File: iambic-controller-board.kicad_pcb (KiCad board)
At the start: 2 copper layers, 48.1 x 15 mm, 16 parts, among them J1 Header 1, J2 AudioJack3, J3 ISP Header, U1 USB_A_PCB, U2 ATtiny85-20S

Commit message: final rev1
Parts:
- added C2: 10uF, Capacitor_SMD:C_0603_1608Metric, F.Cu at (141.2, 103.2)
- D2, D3: value ~ -> BZT52C3V6S
- U1: footprint Custom_Lib:PCB_USB_connector -> Edge_USB_PCB:PCB_USB_A
- moved D1 7.95 mm to (140.6, 101.2)
- moved R1 7.95 mm to (141.5, 101.2)
- moved C1 7.90 mm to (142.3, 104.8)
- moved D3 7.69 mm to (138.3, 99.9), turned to -90 degrees
- moved D4 7.64 mm to (150.3, 106.2)
- moved D5 7.64 mm to (152.3, 106.2)
- moved J1 7.64 mm to (150.2, 96.4)
- moved J2 7.64 mm to (166.7, 102.1)
- moved J3 7.64 mm to (141.2, 107.6)
- moved R2 7.64 mm to (140.9, 99.6)
- moved R3 7.64 mm to (140.9, 98.7)
- moved R4 7.64 mm to (150.3, 108.0)
- moved R5 7.64 mm to (152.3, 108.0)
- moved U2 7.64 mm to (148.5, 102.1)
- moved D2 6.90 mm to (139.3, 98.5)
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- renumbered C5 to C1
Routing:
- net GND: track 73.1 -> 0.12 mm, vias 5 -> 28
- net Net-(D3-K): track 15.9 -> 11.7 mm
- net Net-(D2-K): track 13.4 -> 9.44 mm
- net Net-(D1-A): track 14.2 -> 10.5 mm
- net /MISO: track 24.7 -> 22.4 mm, vias 2 -> 4
- net /AUDIO_TIP: track 34.4 -> 35.7 mm, vias 4 -> 6
- net /USB_DN: track 16.0 -> 16.9 mm, vias 2 -> 1
- net /AUDIO_RING: track 23.8 -> 24.6 mm
- net /USB_DP: track 14.3 -> 14.6 mm, vias 2 -> 0
- net /RESET: track 33.9 -> 33.8 mm, vias 3 -> 6
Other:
- board size 48.1 x 15 mm -> 44.9 x 15 mm
- board text added: "1"
- board text added: "2"
- board text added: "3"
- board text added: "4"
- board text added: "5"
- board text added: "6"
- board text added: "GND"
- board text added: "Iambic Paddle Controller"
- board text added: "P1 RESET"
- board text added: "P2 USB+ ADC2"
- board text added: "P3 USB- ADC3"
- board text added: "P4 MISO DO PWM AIN1"
- board text added: "R"
- board text added: "S"
- board text added: "T"
- board text added: "WayWayWay"
- board text added: "dbstreif"
- board text added: "rev1"

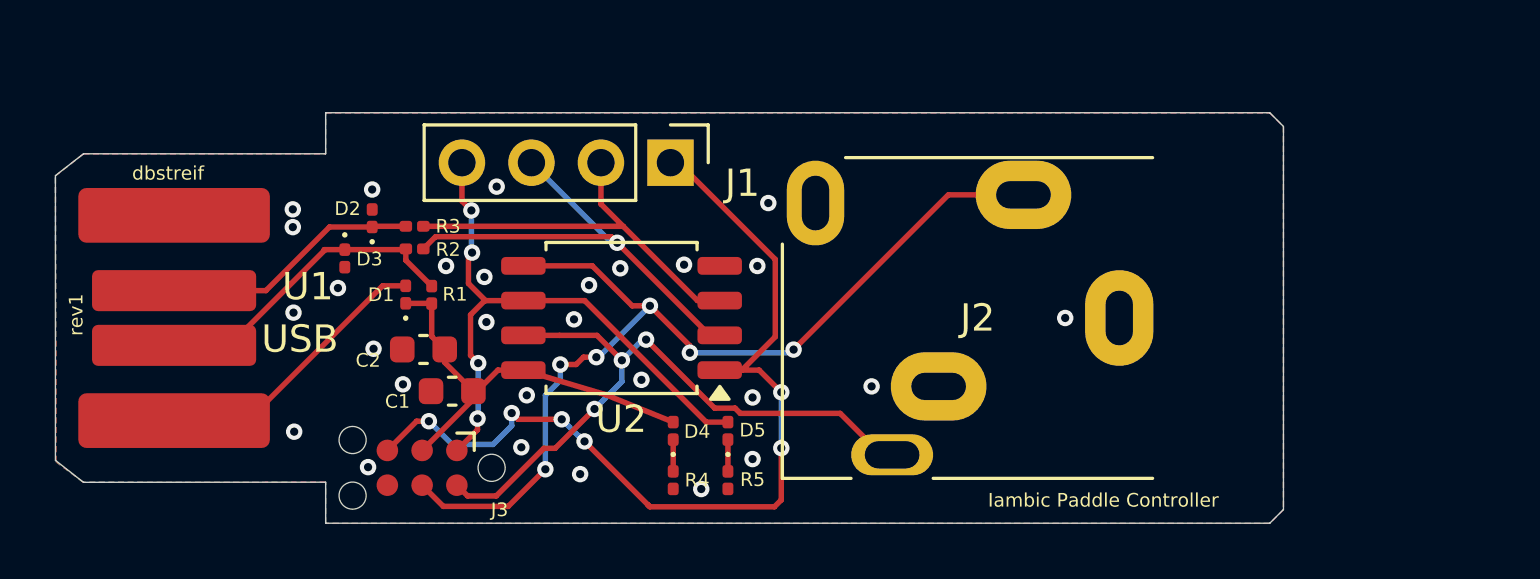
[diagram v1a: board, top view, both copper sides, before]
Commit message: Fixed weird footprints
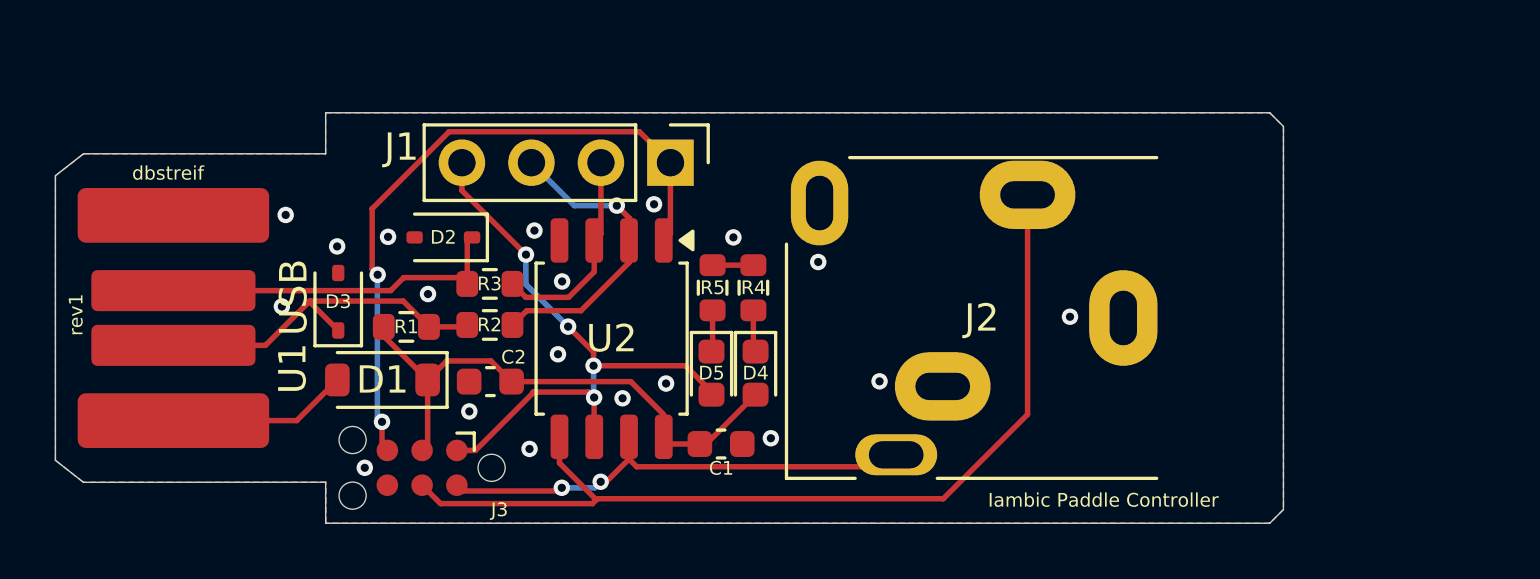
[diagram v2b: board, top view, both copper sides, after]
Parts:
- D1: footprint Diode_SMD:D_0201_0603Metric -> Diode_SMD:D_SOD-123
- D2, D3: value BZT52C3V6S -> 3V6; footprint Diode_SMD:D_0201_0603Metric -> Diode_SMD:D_SOD-323
- D4, D5: footprint LED_SMD:LED_0201_0603Metric -> LED_SMD:LED_0603_1608Metric
- R1, R2, R3, R4, R5: footprint Resistor_SMD:R_0201_0603Metric -> Resistor_SMD:R_0603_1608Metric
- moved C1 10.0 mm to (152.1, 106.7), turned to 180 degrees
- moved R4 7.62 mm to (153.3, 101.0), turned to 90 degrees
- moved R5 7.05 mm to (151.8, 101.0), turned to 90 degrees
- moved R2 3.91 mm to (143.7, 102.3)
- moved D4 3.68 mm to (153.4, 104.1), turned to -90 degrees
- moved R3 3.46 mm to (143.7, 100.8)
- moved D1 3.23 mm to (139.7, 104.4), turned to 180 degrees
- moved C2 2.71 mm to (143.7, 104.4)
- moved D2 2.69 mm to (141.9, 99.2), turned to 180 degrees
- moved D5 2.19 mm to (151.8, 104.1), turned to -90 degrees
- moved D3 1.60 mm to (138.1, 101.5), turned to 90 degrees
- moved R1 1.49 mm to (140.6, 102.4), turned to 0 degrees
- moved U2 0.84 mm to (148.1, 102.8), turned to -90 degrees
- moved J2 0.15 mm to (166.8, 102.1)
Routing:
- net /RESET: track 33.8 -> 25.1 mm, vias 6 -> 2
- net /USB_DP: track 14.6 -> 7.67 mm
- net /AUDIO_RING: track 24.6 -> 17.7 mm, vias 3 -> 2
- net /USB_DN: track 16.9 -> 11.3 mm
- net Net-(D1-A): track 10.5 -> 6.61 mm
- net Net-(D2-K): track 9.44 -> 13.1 mm
- net VCC5V: track 15.7 -> 19.2 mm
- net Net-(D3-K): track 11.7 -> 13.3 mm
- net GND: track 0.12 -> 1.49 mm, vias 28 -> 19
- net /AUDIO_TIP: track 35.7 -> 34.7 mm, vias 6 -> 0

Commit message: fixed route
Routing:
- net GND: vias 19 -> 18
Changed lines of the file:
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@@
-		(net 1)
-	)
-	(via
-		(at 136.050757 101.675)
-		(size 0.6)
-		(drill 0.3)
-		(layers "F.Cu" "B.Cu")
-		(free yes)
 		(net 1)
 	)
@@
 	)
 	(segment
-		(start 132.0875 103.095)
-		(end 135.451 103.095)
+		(start 137.07 101.476)
+		(end 135.8 101.476)
+		(width 0.2)
+		(layer "F.Cu")
+		(net 12)
+	)
+	(segment
+		(start 135.8 101.476)
+		(end 134.181 103.095)
 		(width 0.2)
 		(layer "F.Cu")
@@
 	)
 	(segment
-		(start 135.451 103.095)
-		(end 137.07 101.476)
-		(width 0.2)
-		(layer "F.Cu")
+		(start 134.181 103.095)
+		(end 132.0875 103.095)
+		(width 0.2)
+		(layer "F.Cu")
